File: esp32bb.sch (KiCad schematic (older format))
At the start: 26 parts, among them P1 CONN_01X17, P2 CONN_01X17, P3 USB_OTG, Q1 MMBT3904, Q2 MMBT3904, SW1 SWITCH_SPST, SW2 SWITCH_SPST, U1 ESP32-WROOM, U2 NCP1117ST33T3G, U3 CP2102

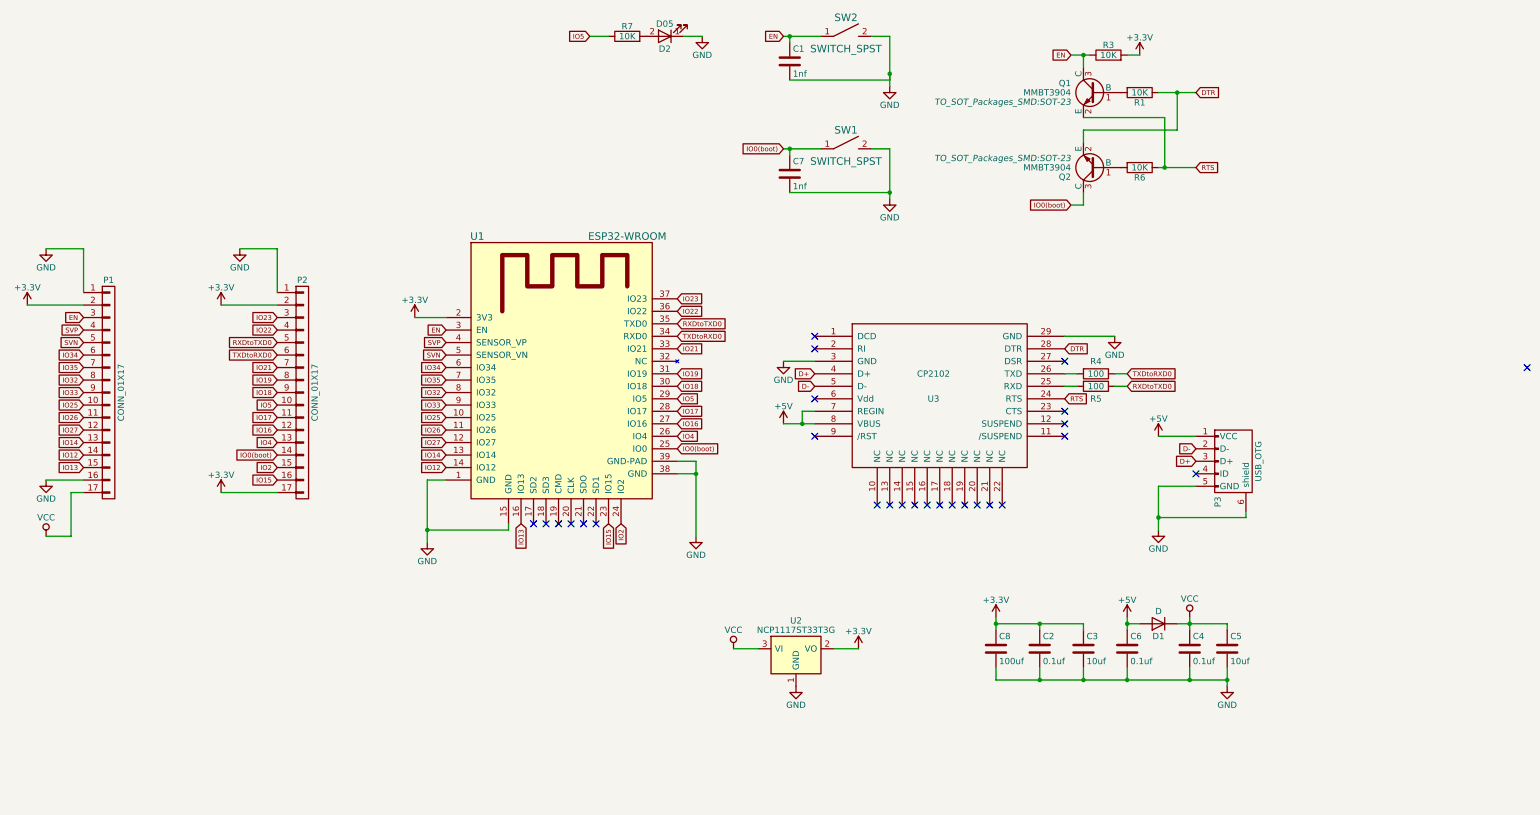
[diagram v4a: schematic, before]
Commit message: Add diode for 3v3 and modify label for registers and condensors
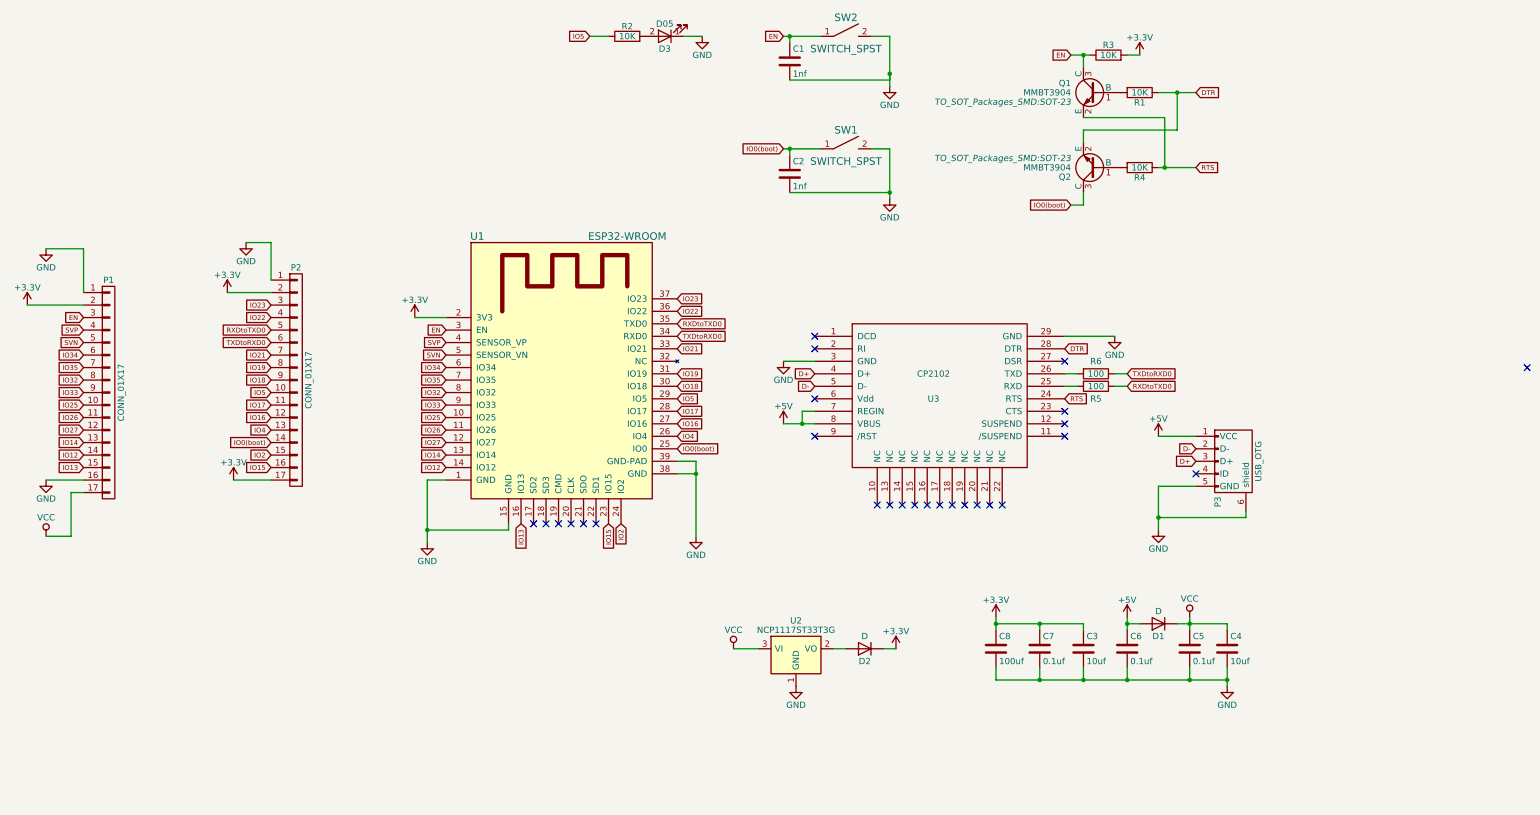
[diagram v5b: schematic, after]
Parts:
- added D2: D, common:D_0805, symbol D
- D1: footprint Diodes_SMD:D_0805 -> common:D_0805
- renumbered C7 to C2, C5 to C4, C4 to C5, C2 to C7, D2 to D3, R7 to R2, R6 to R4, R4 to R6
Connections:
- net +3V3: now also D2.1 (K); no longer U2.2 (VO)
- new net: D2.2 (A), U2.2 (VO)
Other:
- moved on the sheet: P2
